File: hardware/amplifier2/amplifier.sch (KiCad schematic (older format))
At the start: 67 parts, among them IC1 AD8331, IC2 ISL55210, J1 0, P1 5V, P2 3V3, P3 Interface, T1 BALUN, T2 BALUN, U1 MCP4706/16/26, X1 IN_AD, X2 OUT_ISL_B, X3 OUT_AD_B, X4 OUT_AD, X5 IN_ISL, X6 OUT_ISL

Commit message: joined all schemas; added ADC stage; needs footprint assignments and layout
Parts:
- removed P2: 3V3, Pin_Headers:Pin_Header_Angled_1x02, symbol CONN_01X02
- removed X2: OUT_ISL_B, SDRfootprints:1-1337543-0, symbol BNC
- removed X3: OUT_AD_B, SDRfootprints:1-1337543-0, symbol BNC
- removed X4: OUT_AD, SDRfootprints:1-1337543-0, symbol BNC
- removed X5: IN_ISL, SDRfootprints:1-1337543-0, symbol BNC
- removed X6: OUT_ISL, SDRfootprints:1-1337543-0, symbol BNC
- added C?: 10n, symbol C
- added C?: 100u, symbol C
- added C? (x9): 100n, symbol C
- added C?: 22p, symbol C
- added C?: 10p, symbol C
- added C? (x2): 2u2, symbol C
- added C? (x2): 82p, symbol C
- added C? (x3): 180p, symbol C
- added C? (x2): 1u, symbol C
- added C?: TBD, symbol C
- added D? (x2): LED, symbol LED
- added IC?: LP38798, symbol LP38798
- added IC?: LTC2252, symbol LTC2252
- added IC?: NC7SVU04, symbol NC7SVU04
- added JP?: DE0_nano_GPIO-1, symbol DE0_nano_GPIO-1
- added L? (x2): 307n, symbol L_Small
- added L? (x2): 380n, symbol L_Small
- added L? (x2): 390n, symbol L_Small
- added P? (x2): CONN_01X04, symbol CONN_01X04
- added P?: UART, symbol CONN_01X04
- added R? (x4): TBD, Resistors_SMD:R_0603, symbol R
- added R? (x2): 22R, symbol R
- added R? (x2): 0R, symbol R
- added R? (x2): 100, symbol R
- added R?: 3k9, symbol R
- added R?: 23k2, symbol R
- added R?: 13k3, symbol R
- added R? (x2): 10k, symbol R
- added R?: 22k, symbol R
- added R? (x2): 10k, Resistors_SMD:R_0603, symbol R
- added R? (x2): 470, symbol R
- added RP? (x2): R_PACK8, symbol R_PACK8
- added SW?: SW_PUSH, symbol SW_PUSH
- added T? (x2): BALUN, SDRfootprints:CX2041NLT, symbol TRANSFO4
- added W?: CLCK EXT, Measurement_Points:Test_Point_Keystone_5005-5009_Compact, symbol TEST_1P
- added X?: OUT_AD, SDRfootprints:1-1337543-0, symbol BNC
- added X?: IN_ISL, SDRfootprints:1-1337543-0, symbol BNC
- added X?: OUT_ISL, SDRfootprints:1-1337543-0, symbol BNC
- added X?: IN_FILTER, SDRfootprints:1-1337543-0, symbol BNC
- added X?: OUT_FILTER, SDRfootprints:1-1337543-0, symbol BNC
- added X?: IN_ADC, SDRfootprints:1-1337543-0, symbol BNC
- added Y?: FVXO-HC53BR, symbol FVXO-HC53BR
- P3: value Interface -> DAC Interface
- renumbered P1 to P?
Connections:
- net +3.3VADC: now also C?.2, C?.2, IC?.32 (VDD), IC?.7 (VDD), R?.1
- net +3V3: now also C?.2, C?.2, C?.2, IC?.10 (OUT(FB)), IC?.11 (OUT), IC?.12 (OUT), IC?.21 (OVDD), IC?.5 (VCC), JP?.29 (VCC3P3), P?.4 (P4), R?.1, R?.2, Y?.2 (E/D), Y?.6 (VDD)
- net +5V: now also C?.1, IC?.1 (IN), IC?.2 (IN), IC?.3 (IN(CP)), IC?.5 (EN), JP?.11 (VCC_SYS)
- net GNDA: now also C?.1, C?.1, C?.1, C?.1, C?.1, C?.1, C?.1, C?.1, C?.1, C?.2, C?.2, C?.2, D?.1 (K), D?.1 (K), IC?.10 (SHDN), IC?.11 (~OE), IC?.13 (DAP), IC?.20 (OGND), IC?.3 (GND), IC?.6 (GND(CP)), IC?.7 (GND), IC?.8 (GND), IC?.EP (GND), JP?.12 (GND), JP?.30 (GND), P?.1 (P1), R?.1, R?.2, R?.2, SW?.1, T?.2 (PM), T?.2 (PM), X?.2 (Ext), X?.2 (Ext), X?.2 (Ext), X?.2 (Ext), Y?.3 (GND)
- net HILO: now also JP?.6 (GPIO_13)
- net IN2+: now also P?.1 (P1), R?.1
- net IN2-: now also P?.2 (P2), R?.1
- net OUT1+: now also P?.4 (P4)
- net OUT1-: now also P?.3 (P3)
- net OUT2+: now also P?.4 (P4)
- net OUT2-: now also P?.3 (P3)
- net SCL: now also JP?.5 (GPIO_12)
- net SDA: now also JP?.4 (GPIO_11)
- net at T2.1 (PR1), T2.3 (PR2): now also X?.1 (In)
- net at T1.1 (PR1), T1.3 (PR2): now also X?.1 (In)
- new net: C?.1, IC?.4 (CP)
- new net: IC?.8 (FB), R?.1, R?.2
- new net: IC?.9 (SET), R?.2
- new net: T?.1 (PR1), T?.3 (PR2), X?.1 (In) (x2)
- new net: R?.2, T?.4 (S1) (x2)
- new net: R?.2, T?.5 (S2) (x2)
- new net: IC?.1 (AIN+), R?.1
- new net: IC?.12 ((D12)), RP?.1 (P1)
- new net: IC?.13 ((D13)), RP?.2 (P2)
- new net: IC?.14 (D0), RP?.3 (P3)
- new net: IC?.15 (D1), RP?.4 (P4)
- new net: IC?.16 (D2), RP?.5 (P5)
- new net: IC?.17 (D3), RP?.6 (P6)
- new net: IC?.18 (D4), RP?.7 (P7)
- new net: IC?.19 (D5), RP?.8 (P8)
- new net: IC?.2 (AIN-), R?.1
- new net: IC?.22 (D6), RP?.1 (P1)
- new net: IC?.23 (D7), RP?.2 (P2)
- new net: IC?.24 (D8), RP?.3 (P3)
- new net: IC?.25 (D9), RP?.4 (P4)
- new net: IC?.26 (D10), RP?.5 (P5)
- new net: IC?.27 (D11), RP?.6 (P6)
- new net: IC?.28 (OF), RP?.7 (P7)
- new net: IC?.29 (MODE), R?.1, R?.2
- new net: C?.2, C?.2, C?.2, IC?.3 (REFH), IC?.4 (REFH)
- new net: IC?.30 (SENSE), R?.1
- new net: C?.2, IC?.31 (VCM), R?.1, R?.2
- new net: C?.1, C?.1, C?.2, IC?.5 (REFL), IC?.6 (REFL)
- new net: C?.1, L?.2, R?.2, R?.2, R?.2
- new net: C?.2, R?.1, R?.2, R?.2
- new net: C?.2, L?.2, R?.1, R?.1, R?.2
- new net: C?.1, C?.1, L?.1
- new net: C?.1, C?.2, L?.1
- new net: C?.1, L?.1, X?.1 (In)
- new net: C?.2, C?.2, C?.2, C?.2, C?.2, X?.2 (Ext), X?.2 (Ext)
- new net: C?.1, L?.2, X?.1 (In)
- new net: C?.1, L?.1, L?.2 (x3)
- new net: R?.1, R?.2, Y?.1 (VC)
- new net: D?.2 (A), R?.2 (x2)
- new net CLK: JP?.1 (GPIO_1_IN0), RP?.9 (R8)
- new net CLK_EXTERNAL: IC?.4 (Y), RP?.8 (P8), W?.1
- new net CLK_INTERNAL: IC?.2 (A), Y?.4 (OUT)
- new net D0: JP?.28 (GPIO_123), RP?.14 (R3)
- new net D1: JP?.26 (GPIO_121), RP?.13 (R4)
- new net D10: JP?.13 (GPIO_18), RP?.12 (R5)
- new net D11: JP?.10 (GPIO_17), RP?.11 (R6)
- new net D12: JP?.36 (GPIO_129), RP?.16 (R1)
- new net D13: JP?.31 (GPIO_124), RP?.15 (R2)
- new net D2: JP?.24 (GPIO_119), RP?.12 (R5)
- new net D3: JP?.23 (GPIO_118), RP?.11 (R6)
- new net D4: JP?.22 (GPIO_117), RP?.10 (R7)
- new net D5: JP?.21 (GPIO_116), RP?.9 (R8)
- new net D6: JP?.19 (GPIO_114), RP?.16 (R1)
- new net D7: JP?.17 (GPIO_112), RP?.15 (R2)
- new net D8: JP?.16 (GPIO_111), RP?.14 (R3)
- new net D9: JP?.14 (GPIO_19), RP?.13 (R4)
- new net IN3+: C?.2, P?.1 (P1), R?.1
- new net IN3-: C?.2, P?.2 (P2), R?.1
- new net LED1: JP?.40 (GPIO_133), R?.1
- new net LED2: JP?.39 (GPIO_132), R?.1
- new net OF: JP?.9 (GPIO_16), RP?.10 (R7)
- new net RX: JP?.37 (GPIO_130), P?.3 (P3)
- new net SW1: C?.1, JP?.7 (GPIO_14), R?.1, SW?.2
- new net TX: JP?.38 (GPIO_131), P?.2 (P2)
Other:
- note added: "0402 is important\naccording to DS"
- note added: "ADC"
- note added: "Amplifier Stage"
- note added: "Analog Filter"
- note added: "Clock Buffer"
- note added: "Clock Generator"
- note added: "Connectors for stage testing"
- note added: "DESIGN CONSIDERATIONS\n- No Ground under IO Pins\n- Only ONE GND-Plane"
- note added: "GND: offset binary, stabilizer off\n1/3 VDD: offset binary, stabilizer on\n2/3 VDD: 2’s complement, stabilizer on\nVDD: 2’s complement, stabilizer off"
- note added: "Power Supply"
- note added: "Stabilisator Caps for LTC2252"
- note removed: "DESIGN CONSIDERATIONS\n- No Ground under IO Pins\n- Only ON GND-Plane"
- moved on the sheet: C1, C10, C11, C12, C13, C14, C15, C16, C17, C18, C19, C2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

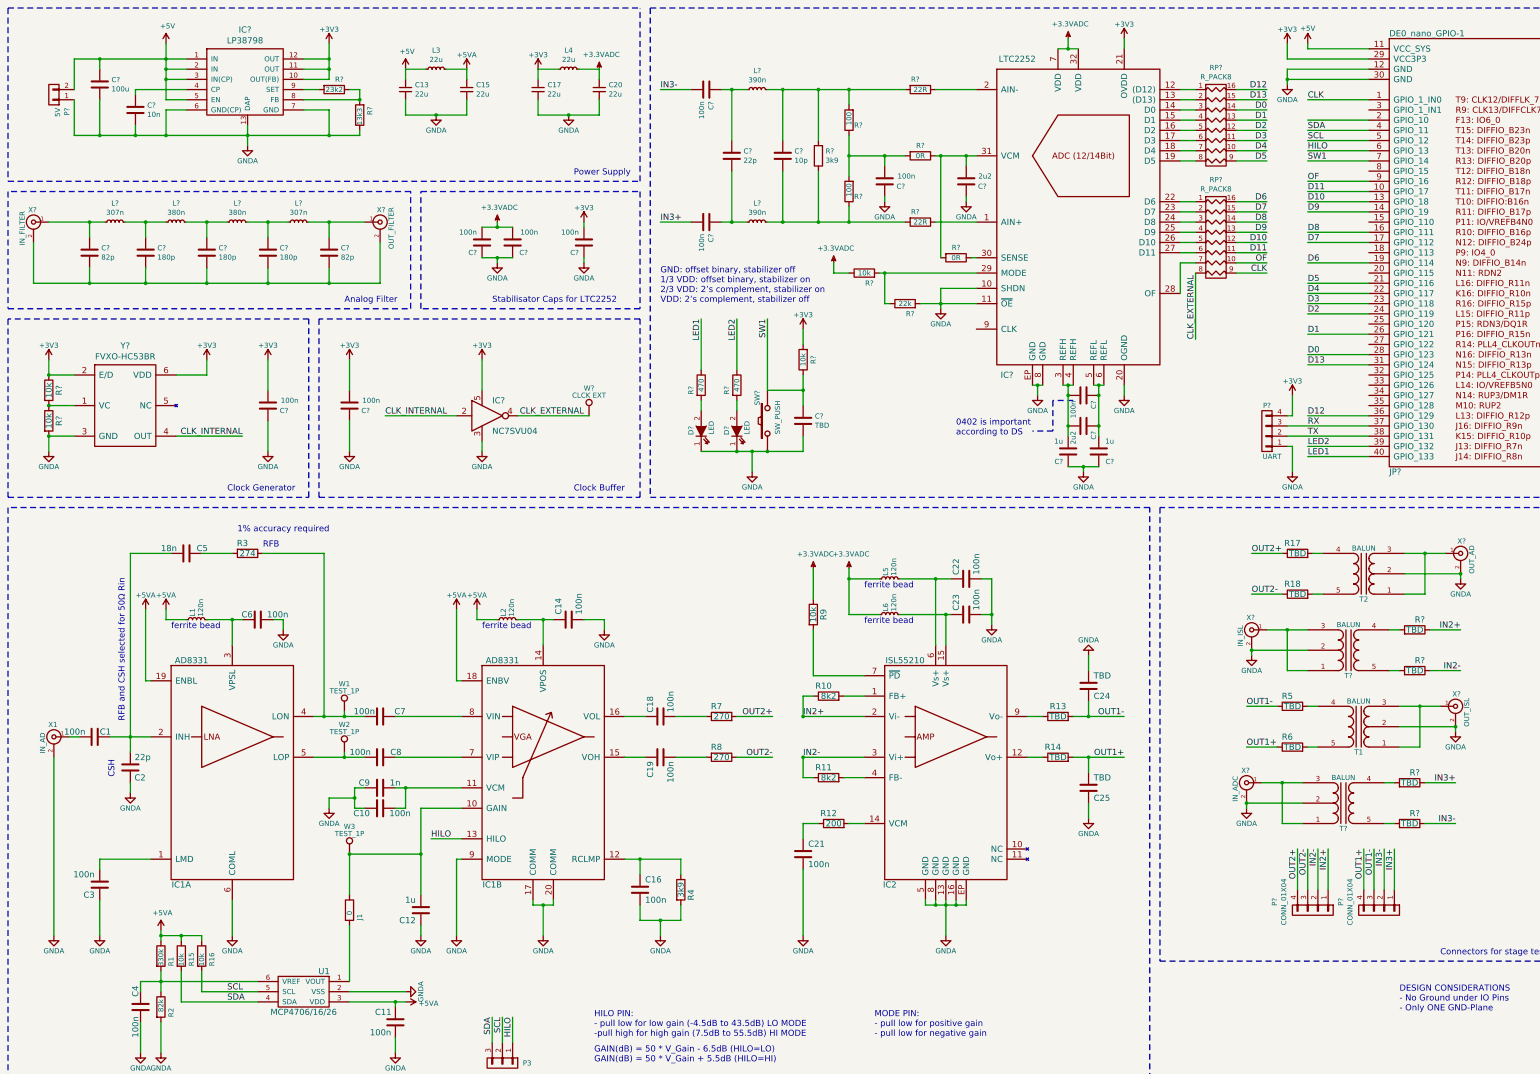
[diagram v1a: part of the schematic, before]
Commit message: rerouting nearly done; added remaining footprints
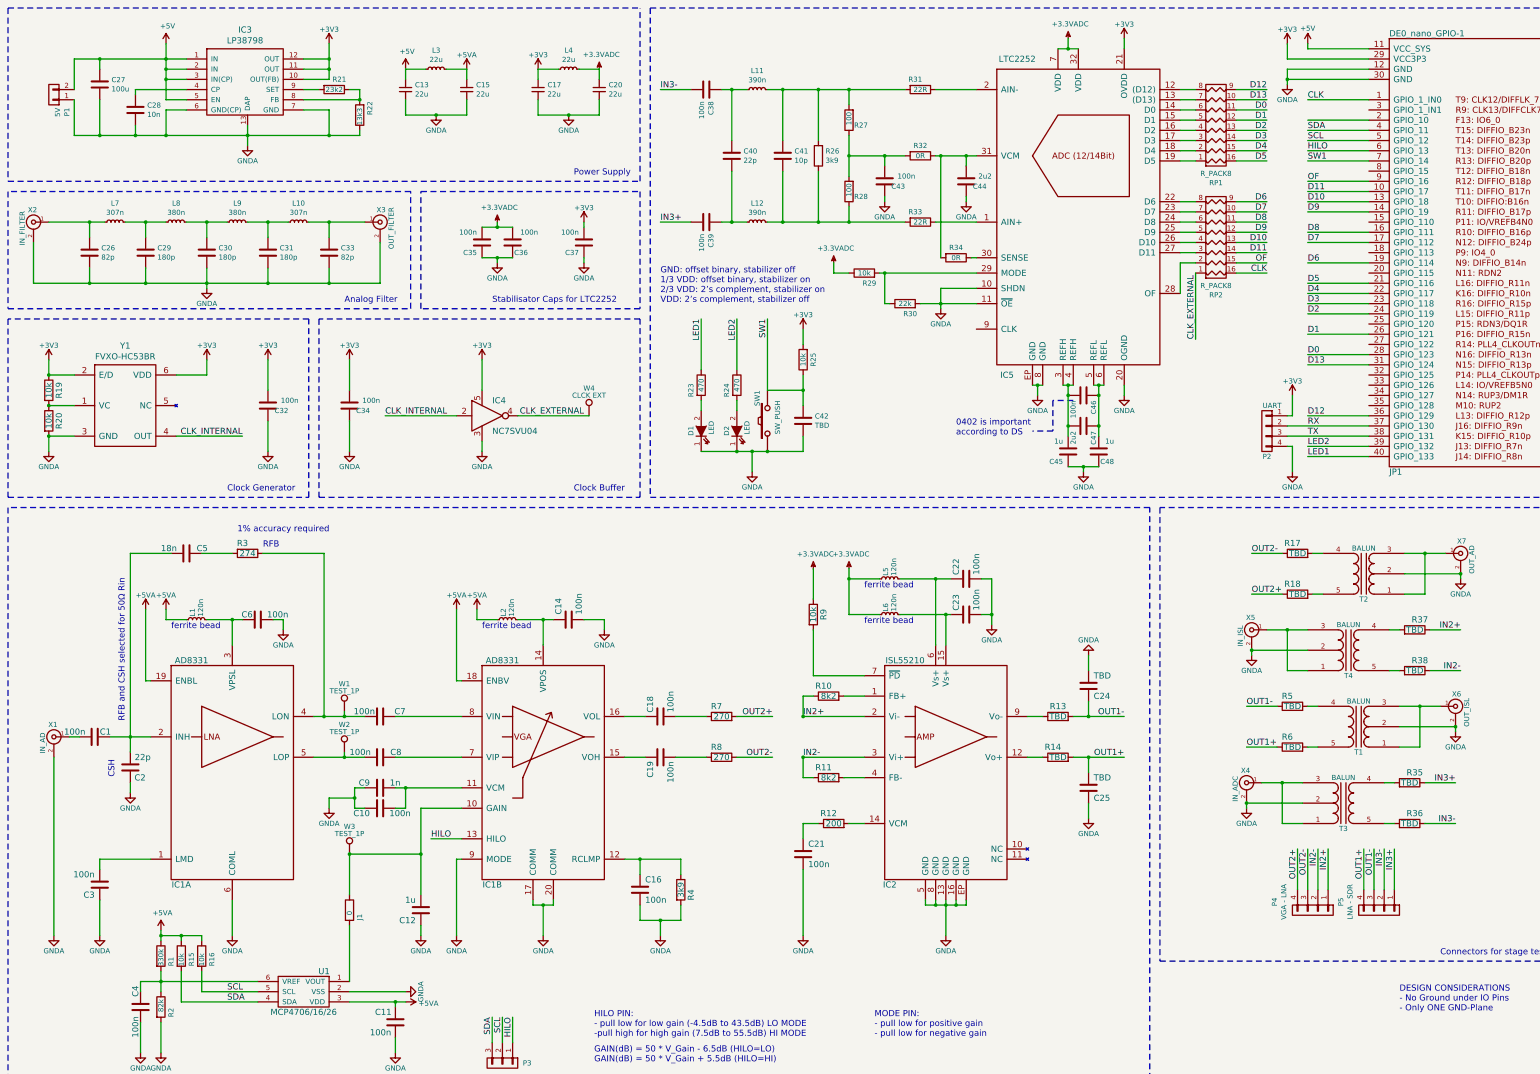
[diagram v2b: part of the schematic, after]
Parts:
- C26, C27, C28, C29, C30, C31, C32, C33, C34, C35, C36, C37, C38, C39, C40, C41, C42, C43, C44, C45, C47, C48: renamed from C?; footprint (none) -> Capacitors_SMD:C_0603
- C46: renamed from C?; footprint (none) -> Capacitors_SMD:C_0402
- D1, D2: renamed from D?; footprint (none) -> LEDs:LED_0603
- IC4: renamed from IC?; footprint (none) -> SDRfootprints:SOT353
- IC5: renamed from IC?; footprint (none) -> Housings_DFN_QFN:QFN-32-1EP_5x5mm_Pitch0.5mm
- JP1: renamed from JP?; footprint (none) -> Pin_Headers:Pin_Header_Angled_2x20
- L10, L7, L8, L9: renamed from L?; footprint (none) -> SDRfootprints:Coil_132-XXSM_L_
- L11, L12: renamed from L?; footprint (none) -> SDRfootprints:1008
- P1: renamed from P?; footprint Pin_Headers:Pin_Header_Angled_1x02 -> Connect:bornier2
- P2: renamed from P?; footprint (none) -> Connectors_Molex:Molex_PicoBlade_53398-0471_04x1.25mm_Straight
- P4: renamed from P?; value CONN_01X04 -> VGA - LNA; footprint (none) -> Connect:bornier4
- P5: renamed from P?; value CONN_01X04 -> LNA - SDR; footprint (none) -> Connect:bornier4
- R21, R22, R23, R24, R25, R26, R27, R28, R29, R30, R31, R32, R33, R34: renamed from R?; footprint (none) -> Resistors_SMD:R_0603
- RP1, RP2: renamed from RP?; footprint (none) -> SDRfootprints:2406
- SW1: renamed from SW?; footprint (none) -> Buttons_Switches_SMD:SW_SPST_PTS645
- Y1: renamed from Y?; footprint (none) -> SDRfootprints:OSC_631-1265-1-ND
- gave numbers to parts that had none: 16
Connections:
- net +3V3: now also P2.1 (P1); no longer P2.4 (P4)
- net CLK: now also RP2.16 (R1); no longer RP2.9 (R8)
- net CLK_EXTERNAL: now also RP2.1 (P1); no longer RP2.8 (P8)
- net D0: now also RP1.11 (R6); no longer RP1.14 (R3)
- net D1: now also RP1.12 (R5); no longer RP1.13 (R4)
- net D10: now also RP2.13 (R4); no longer RP2.12 (R5)
- net D11: now also RP2.14 (R3); no longer RP2.11 (R6)
- net D12: now also RP1.9 (R8); no longer RP1.16 (R1)
- net D13: now also RP1.10 (R7); no longer RP1.15 (R2)
- net D2: now also RP1.13 (R4); no longer RP1.12 (R5)
- net D3: now also RP1.14 (R3); no longer RP1.11 (R6)
- net D4: now also RP1.15 (R2); no longer RP1.10 (R7)
- net D5: now also RP1.16 (R1); no longer RP1.9 (R8)
- net D6: now also RP2.9 (R8); no longer RP2.16 (R1)
- net D7: now also RP2.10 (R7); no longer RP2.15 (R2)
- net D8: now also RP2.11 (R6); no longer RP2.14 (R3)
- net D9: now also RP2.12 (R5); no longer RP2.13 (R4)
- net GNDA: now also C26.2, C29.2, C30.2, C31.2, C33.2, P2.4 (P4), X2.2 (Ext), X3.2 (Ext); no longer P2.1 (P1)
- net OF: now also RP2.15 (R2); no longer RP2.10 (R7)
- net OUT2+: now also R18.1; no longer R17.1
- net OUT2-: now also R17.1; no longer R18.1
- net RX: now also P2.2 (P2); no longer P2.3 (P3)
- net TX: now also P2.3 (P3); no longer P2.2 (P2)
- net at IC5.12 ((D12)): now also RP1.8 (P8); no longer RP1.1 (P1)
- net at IC5.13 ((D13)): now also RP1.7 (P7); no longer RP1.2 (P2)
- net at IC5.14 (D0): now also RP1.6 (P6); no longer RP1.3 (P3)
- net at IC5.15 (D1): now also RP1.5 (P5); no longer RP1.4 (P4)
- net at IC5.16 (D2): now also RP1.4 (P4); no longer RP1.5 (P5)
- net at IC5.17 (D3): now also RP1.3 (P3); no longer RP1.6 (P6)
- net at IC5.18 (D4): now also RP1.2 (P2); no longer RP1.7 (P7)
- net at IC5.19 (D5): now also RP1.1 (P1); no longer RP1.8 (P8)
- net at IC5.22 (D6): now also RP2.8 (P8); no longer RP2.1 (P1)
- net at IC5.23 (D7): now also RP2.7 (P7); no longer RP2.2 (P2)
- net at IC5.24 (D8): now also RP2.6 (P6); no longer RP2.3 (P3)
- net at IC5.25 (D9): now also RP2.5 (P5); no longer RP2.4 (P4)
- net at IC5.26 (D10): now also RP2.4 (P4); no longer RP2.5 (P5)
- net at IC5.27 (D11): now also RP2.3 (P3); no longer RP2.6 (P6)
- net at IC5.28 (OF): now also RP2.2 (P2); no longer RP2.7 (P7)

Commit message: last state; minor changes still to do; powersupply missing; outline missing
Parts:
- removed W4: CLCK EXT, Measurement_Points:Test_Point_Keystone_5005-5009_Compact, symbol TEST_1P
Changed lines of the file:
@@
 	1    0    0    -1
 $EndComp
-Text Label 6200 4550 2    60   ~ 0
+Text Label 6250 4550 2    60   ~ 0
 CLK_EXTERNAL
 $Comp
@@
 Clock Buffer
 $Comp
-L TEST_1P W4
-U 1 1 58260A20
-P 6250 4550
-F 0 "W4" H 6250 4820 50  0000 C CNN
-F 1 "CLCK EXT" H 6250 4750 50  0000 C CNN
-F 2 "Measurement_Points:Test_Point_Keystone_5005-5009_Compact" H 6450 4550 50  0001 C CNN
-F 3 "" H 6450 4550 50  0000 C CNN
-	1    6250 4550
-	1    0    0    -1
-$EndComp
-$Comp
 L C C34

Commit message: all routing but PSU done; maybe schema needs nicer annotations
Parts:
- removed P3: DAC Interface, Pin_Headers:Pin_Header_Angled_1x03, symbol CONN_01X03
- P1: footprint Connect:bornier2 -> SDRfootprints:ED365-2
- P4, P5: footprint Connect:bornier4 -> SDRfootprints:ED365-4
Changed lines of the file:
@@
 F 0 "P1" V 872 1528 50  0000 L CNN
 F 1 "5V" V 963 1528 50  0000 L CNN
-F 2 "Connect:bornier2" H 1000 1400 50  0001 C CNN
+F 2 "SDRfootprints:ED365-2" H 1000 1400 50  0001 C CNN
 F 3 "" H 1000 1400 50  0000 C CNN
 	1    1000 1400
 	-1   0    0    1
 $EndComp
-$Comp
-L CONN_01X03 P3
-U 1 1 5812C38D
-P 5400 10900
-F 0 "P3" V 5400 11100 50  0000 L CNN
-F 1 "DAC Interface" V 5550 10750 50  0000 L CNN
-F 2 "Pin_Headers:Pin_Header_Angled_1x03" H 5400 10900 50  0001 C CNN
-F 3 "" H 5400 10900 50  0000 C CNN
-	1    5400 10900
-	0    1    1    0
-$EndComp
-Text Label 5400 10450 3    60   ~ 0
-SCL
-Text Label 5300 10450 3    60   ~ 0
-SDA
-Text Label 5500 10450 3    60   ~ 0
-HILO
 $Comp
 L R R15
@@
 F 0 "P4" H 13269 9025 50  0000 C CNN
 F 1 "VGA - LNA" H 13269 9116 50  0000 C CNN
-F 2 "Connect:bornier4" H 13350 9400 50  0001 C CNN
+F 2 "SDRfootprints:ED365-4" H 13350 9400 50  0001 C CNN
 F 3 "" H 13350 9400 50  0000 C CNN
 	1    13350 9400
@@
 F 0 "P5" H 13919 9025 50  0000 C CNN
 F 1 "LNA - SDR" H 13919 9116 50  0000 C CNN
-F 2 "Connect:bornier4" H 14000 9400 50  0001 C CNN
+F 2 "SDRfootprints:ED365-4" H 14000 9400 50  0001 C CNN
 F 3 "" H 14000 9400 50  0000 C CNN
 	1    14000 9400
@@
 	3900 9550 3900 10100
 Wire Wire Line
-	5300 10450 5300 10700
-Wire Wire Line
-	5400 10450 5400 10700
-Wire Wire Line
-	5500 10450 5500 10700
-Wire Wire Line
 	2250 10000 2250 10300
